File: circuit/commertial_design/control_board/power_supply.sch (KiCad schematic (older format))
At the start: 31 parts, among them Q1 2SB647, Q2 2SK3611, U1 MC34063A, U2 MC34063A

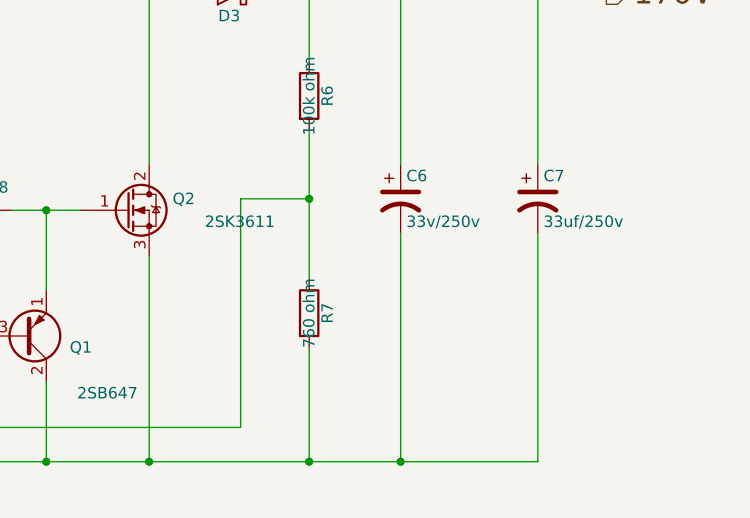
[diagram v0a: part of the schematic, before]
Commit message: Layout need to be arranged, scheme is finished
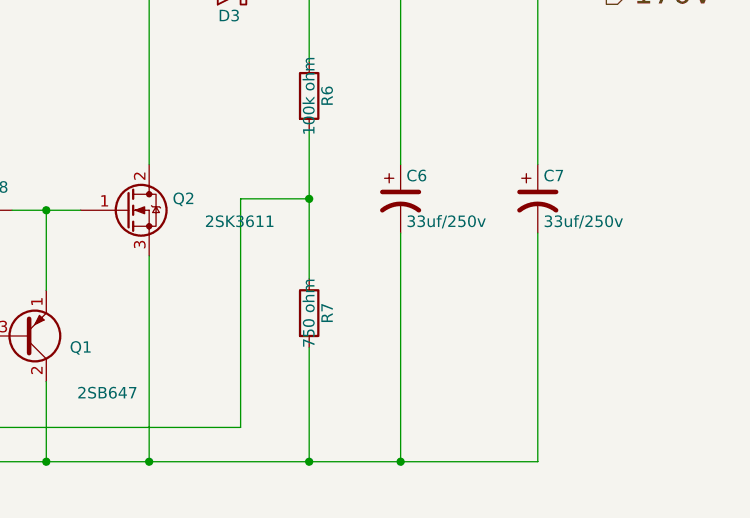
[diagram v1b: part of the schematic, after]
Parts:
- C6: value 33v/250v -> 33uf/250v
- R7: value 760 ohm -> 750 ohm
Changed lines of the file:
@@
 P 8150 4700
 F 0 "C6" H 8175 4800 50  0000 L CNN
-F 1 "33v/250v" H 8175 4600 50  0000 L CNN
+F 1 "33uf/250v" H 8175 4600 50  0000 L CNN
 F 2 "Capacitors_ThroughHole:C_Radial_D13_L21_P5" H 8150 4700 60  0001 C CNN
 F 3 "" H 8150 4700 60  0000 C CNN
@@
 P 7750 5200
 F 0 "R7" V 7830 5200 50  0000 C CNN
-F 1 "760 ohm" V 7750 5200 50  0000 C CNN
+F 1 "750 ohm" V 7750 5200 50  0000 C CNN
 F 2 "Resistors_SMD:R_1206_HandSoldering" V 7680 5200 30  0001 C CNN
 F 3 "" H 7750 5200 30  0000 C CNN

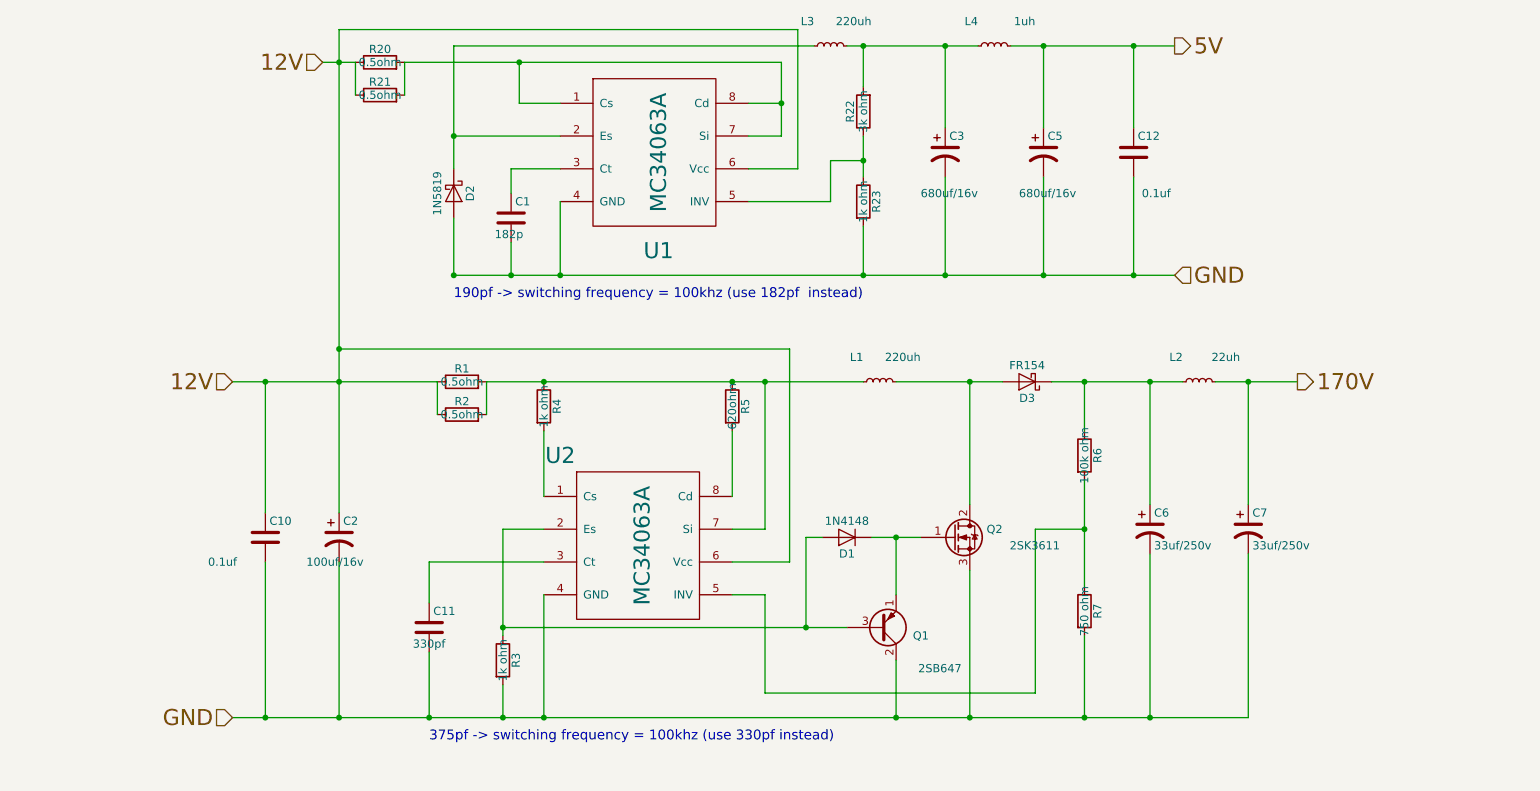
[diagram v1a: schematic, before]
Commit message: Add ratio extender circuit
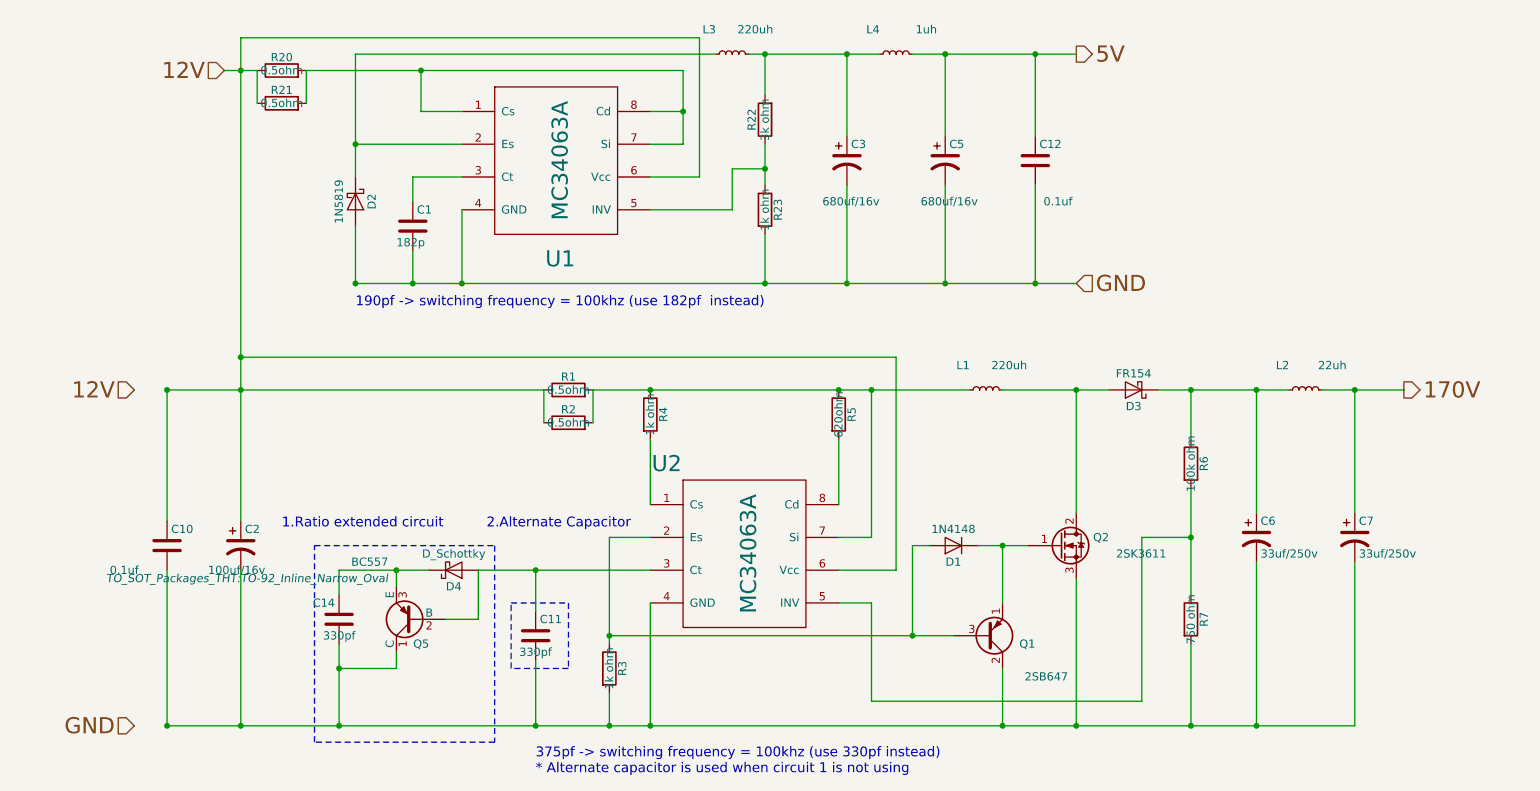
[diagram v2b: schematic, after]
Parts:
- added C14: 330pf, Capacitors_SMD:C_0805_HandSoldering, symbol C
- added D4: D_Schottky, Diodes_ThroughHole:Diode_DO-35_SOD27_Horizontal_RM10, symbol D_Schottky
- added Q5: BC557, TO_SOT_Packages_THT:TO-92_Inline_Narrow_Oval, symbol BC557
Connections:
- net GND: no longer C10.2, C11.2, C2.2, C6.2, C7.2, Q1.2 (C), Q2.3 (S), R3.2, R7.2, U2.4 (GND)
- net at C11.1, U2.3 (Ct): now also D4.2 (A), Q5.2 (B)
- new net: C10.2, C11.2, C14.2, C2.2, C6.2, C7.2, Q1.2 (C), Q2.3 (S), Q5.1 (C), R3.2, R7.2, U2.4 (GND)
- new net: C14.1, D4.1 (K), Q5.3 (E)
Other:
- note added: "1.Ratio extended circuit"
- note added: "2.Alternate Capacitor"
- note added: "375pf -> switching frequency = 100khz (use 330pf instead)\n* Alternate capacitor is used when circuit 1 is not using"
- note removed: "375pf -> switching frequency = 100khz (use 330pf instead)"
- moved on the sheet: C1, C10, C11, C12, C2, C3, C5, C6, C7, D1, D2, D3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

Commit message: Fix PCB board
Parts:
- removed C11: 330pf, Capacitors_SMD:C_0805_HandSoldering, symbol C
- Q5: footprint TO_SOT_Packages_THT:TO-92_Inline_Narrow_Oval -> TO-92_
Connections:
- net GND: now also C10.2, C14.2, C2.2, C6.2, C7.2, Q1.2 (C), Q2.3 (S), Q5.1 (C), R3.2, R7.2, U2.4 (GND)
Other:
- note added: "375pf -> switching frequency = 100khz (use 330pf instead)"
- note added: "Ratio extended circuit"
- note removed: "1.Ratio extended circuit"
- note removed: "2.Alternate Capacitor"
- note removed: "375pf -> switching frequency = 100khz (use 330pf instead)\n* Alternate capacitor is used when circuit 1 is not using"
- moved on the sheet: C14, D4, Q5
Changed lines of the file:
@@
 12V
-$Comp
-L C C11
-U 1 1 573F0108
-P 4400 5350
-F 0 "C11" H 4425 5450 50  0000 L CNN
-F 1 "330pf" H 4300 5250 50  0000 L CNN
-F 2 "Capacitors_SMD:C_0805_HandSoldering" H 4438 5200 30  0001 C CNN
-F 3 "" H 4400 5350 60  0000 C CNN
-	1    4400 5350
-	1    0    0    -1
-$EndComp
 $Comp
 L R R22
@@
 Text Notes 3300 3350 0    60   ~ 0
 190pf -> switching frequency = 100khz (use 182pf  instead)
-Text Notes 4400 6200 0    60   ~ 0
-375pf -> switching frequency = 100khz (use 330pf instead)\n* Alternate capacitor is used when circuit 1 is not using
+Text Notes 3250 6150 0    60   ~ 0
+375pf -> switching frequency = 100khz (use 330pf instead)
 $Comp
 L C C12
@@
 L BC557 Q5
 U 1 1 57D6CA32
-P 3650 5250
-F 0 "Q5" H 3550 5400 50  0000 L CNN
-F 1 "BC557" H 3800 4900 50  0000 L CNN
-F 2 "TO_SOT_Packages_THT:TO-92_Inline_Narrow_Oval" H 3800 5000 50  0000 L CIN
-F 3 "" H 3650 5250 50  0000 L CNN
-	1    3650 5250
+P 3850 5250
+F 0 "Q5" H 3750 5400 50  0000 L CNN
+F 1 "BC557" H 4000 4900 50  0000 L CNN
+F 2 "TO-92_" H 3350 5650 50  0001 L CIN
+F 3 "" H 3850 5250 50  0000 L CNN
+	1    3850 5250
 	-1   0    0    1
 $EndComp
@@
 L D_Schottky D4
 U 1 1 57D6CACB
-P 3900 4950
-F 0 "D4" H 3900 5050 50  0000 C CNN
-F 1 "D_Schottky" H 3900 4850 50  0000 C CNN
-F 2 "Diodes_ThroughHole:Diode_DO-35_SOD27_Horizontal_RM10" H 3900 4950 50  0001 C CNN
-F 3 "" H 3900 4950 50  0000 C CNN
-	1    3900 4950
+P 4150 4950
+F 0 "D4" H 4150 5050 50  0000 C CNN
+F 1 "D_Schottky" H 4150 4850 50  0000 C CNN
+F 2 "Diodes_ThroughHole:Diode_DO-35_SOD27_Horizontal_RM10" H 4150 4950 50  0001 C CNN
+F 3 "" H 4150 4950 50  0000 C CNN
+	1    4150 4950
 	1    0    0    1
 $EndComp
@@
 L C C14
 U 1 1 57D6CE9A
-P 3200 5250
-F 0 "C14" H 3225 5350 50  0000 L CNN
-F 1 "330pf" H 3100 5150 50  0000 L CNN
-F 2 "Capacitors_SMD:C_0805_HandSoldering" H 3238 5100 30  0001 C CNN
-F 3 "" H 3200 5250 60  0000 C CNN
-	1    3200 5250
+P 3500 5250
+F 0 "C14" H 3525 5350 50  0000 L CNN
+F 1 "330pf" H 3400 5150 50  0000 L CNN
+F 2 "Capacitors_SMD:C_0805_HandSoldering" H 3538 5100 30  0001 C CNN
+F 3 "" H 3500 5250 60  0000 C CNN
+	1    3500 5250
 	-1   0    0    -1
 $EndComp
@@
 Connection ~ 2600 3850
 Wire Wire Line
-	2600 4950 2600 5900
+	2600 5900 2600 4950
 Connection ~ 2600 5900
 Wire Wire Line
-	2150 3850 4450 3850
+	1950 3850 4450 3850
 Wire Wire Line
 	7100 4800 7400 4800
@@
 	7250 3850 7900 3850
 Wire Wire Line
-	2150 5900 9400 5900
-Wire Wire Line
-	4400 5200 4400 4950
-Wire Wire Line
-	4400 5500 4400 5900
-Connection ~ 4400 5900
-Wire Wire Line
-	4050 4950 5100 4950
+	1950 5900 9400 5900
 Wire Wire Line
 	3650 2550 3650 2700
@@
 Connection ~ 2150 5900
 Wire Wire Line
-	3750 4950 3200 4950
-Wire Wire Line
-	3550 4950 3550 5050
-Wire Wire Line
-	3850 5250 4050 5250
-Wire Wire Line
-	4050 5250 4050 4950
-Wire Wire Line
-	3200 4950 3200 5100
-Connection ~ 3550 4950
-Wire Wire Line
-	3550 5450 3550 5550
-Wire Wire Line
-	3550 5550 3200 5550
-Wire Wire Line
-	3200 5400 3200 5900
-Connection ~ 4400 4950
-Connection ~ 3200 5900
-Connection ~ 3200 5550
-Text Notes 2850 4700 0    60   ~ 0
-1.Ratio extended circuit
+	3500 4950 4000 4950
+Wire Wire Line
+	3750 4950 3750 5050
+Wire Wire Line
+	4050 5250 4350 5250
+Wire Wire Line
+	3500 4950 3500 5100
+Connection ~ 3750 4950
+Wire Wire Line
+	3750 5450 3750 5500
+Wire Wire Line
+	3750 5500 3500 5500
+Wire Wire Line
+	3500 5400 3500 5900
+Connection ~ 3500 5900
+Connection ~ 3500 5500
 Wire Notes Line
-	3050 4800 4150 4800
+	3300 4800 4400 4800
 Wire Notes Line
-	4150 4800 4150 6000
+	4400 4800 4400 6000
 Wire Notes Line
-	4150 6000 3050 6000
+	4400 6000 3300 6000
 Wire Notes Line
-	3050 6000 3050 4800
-Wire Notes Line
-	4250 5150 4600 5150
-Wire Notes Line
-	4600 5150 4600 5550
-Wire Notes Line
-	4600 5550 4250 5550
-Wire Notes Line
-	4250 5550 4250 5150
-Text Notes 4100 4700 0    60   ~ 0
-2.Alternate Capacitor
+	3300 6000 3300 4800
+Wire Wire Line
+	4300 4950 5100 4950
+Wire Wire Line
+	4350 5250 4350 4950
+Connection ~ 4350 4950
+Text Notes 3300 4750 0    60   ~ 0
+Ratio extended circuit
 $EndSCHEMATC

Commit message: Fix board errors
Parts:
- added C11, C16: 10uf, Capacitors_SMD:C_0805_HandSoldering, symbol C
- added U10: LM1117-3.3, TO_SOT_Packages_SMD:SOT-223, symbol LM1117-3.3
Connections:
- net 5V: now also C11.1, U10.3 (VI)
- net GND: now also C11.2, C16.2, U10.1 (GND/ADJ)
- new net 3V3: C16.1, U10.2 (VO), U10.4 (VO)
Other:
- moved on the sheet: C1, C10, C12, C14, C2, C3, C5, C6, C7, D1, D2, D3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

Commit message: Give part name (D_Schotkky)
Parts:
- D4: value D_Schottky -> 1N5819 (Replacement for D_Schottky)
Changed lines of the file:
@@
 P 3600 5250
 F 0 "Q5" H 3500 5400 50  0000 L CNN
-F 1 "BC557" H 3750 4900 50  0000 L CNN
+F 1 "BC557" H 3400 5500 50  0000 L CNN
 F 2 "TO-92_" H 3100 5650 50  0001 L CIN
 F 3 "" H 3600 5250 50  0000 L CNN
@@
 P 3900 4950
 F 0 "D4" H 3900 5050 50  0000 C CNN
-F 1 "D_Schottky" H 3900 4850 50  0000 C CNN
+F 1 "1N5819 (Replacement for D_Schottky)" H 3850 4850 50  0000 C CNN
 F 2 "Diodes_ThroughHole:Diode_DO-35_SOD27_Horizontal_RM10" H 3900 4950 50  0001 C CNN
 F 3 "" H 3900 4950 50  0000 C CNN
